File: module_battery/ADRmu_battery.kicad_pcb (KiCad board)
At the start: 2 copper layers, 160 x 100 mm, 81 parts, among them J101 Harting 09042326831, Q101 Q_NMOS_GDS, Q102 Q_NMOS_GDS, Q103 MMBFJ111, Q104 MMBFJ111, Q105 MMBFJ111, Q106 MMBFJ111, U101 BQ7791500, U102 LTC4079, U103 L7812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

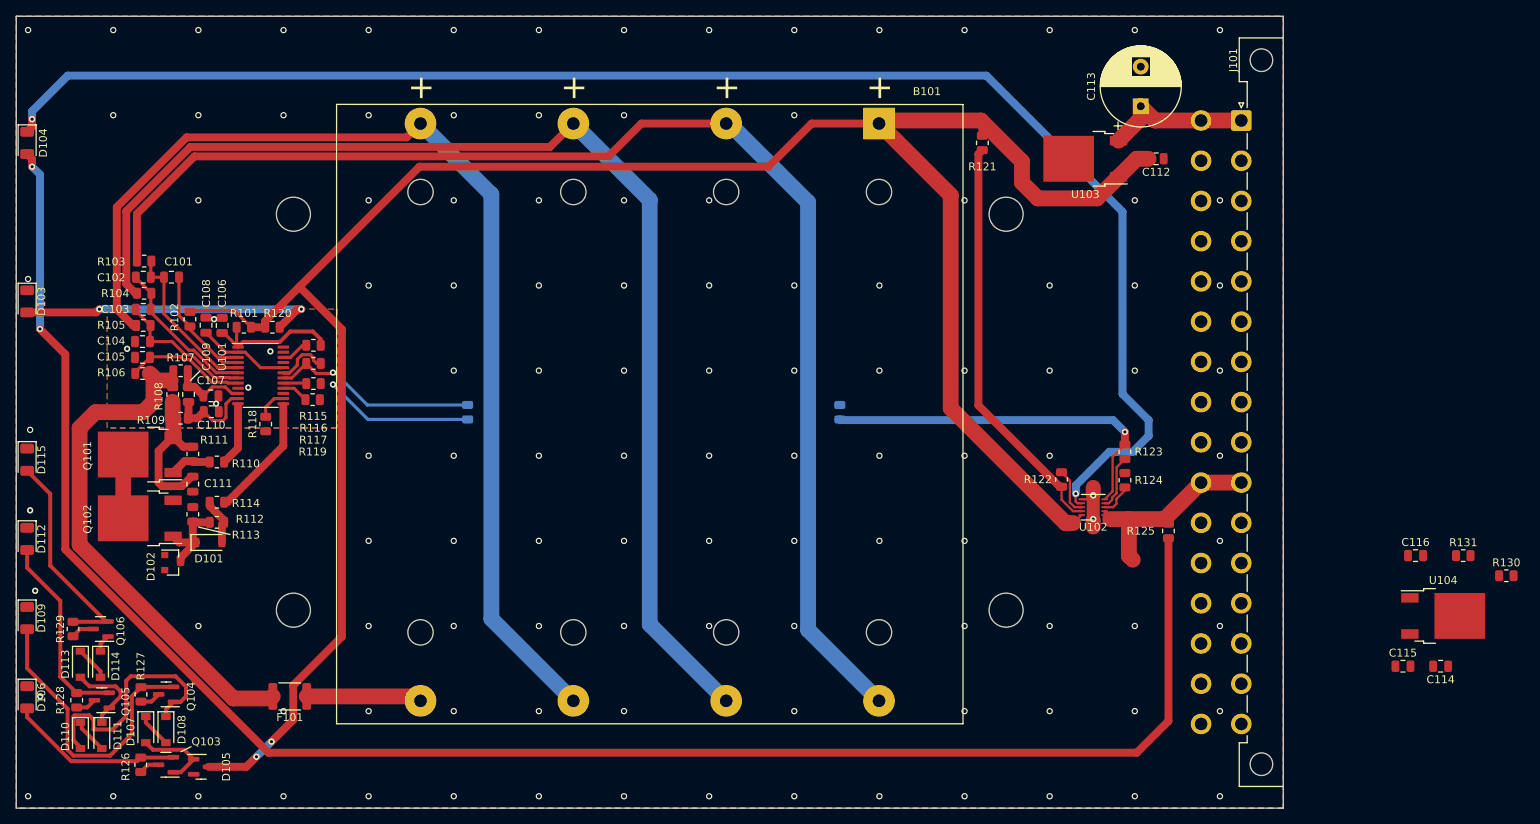
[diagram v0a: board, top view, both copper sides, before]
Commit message: battery module rev 0.3 routed
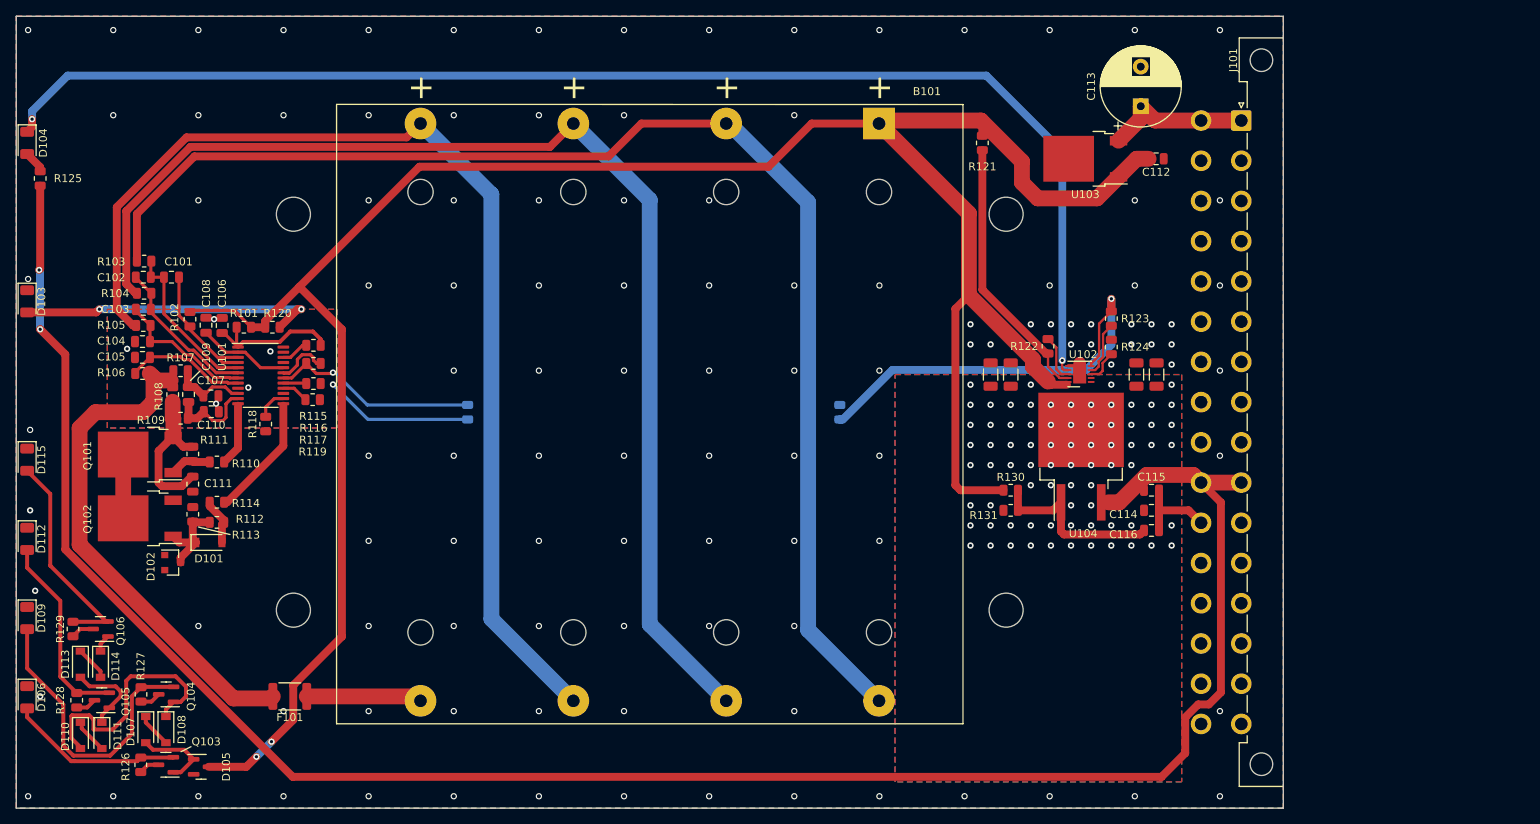
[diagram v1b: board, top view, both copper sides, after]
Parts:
- added HS101: THJP1206AST1, Capacitor_SMD:C_1206_3216Metric, F.Cu at (193.0, 95.2)
- added HS102: THJP1206AST1, Capacitor_SMD:C_1206_3216Metric, F.Cu at (195.6, 95.2)
- added HS103: THJP1206AST1, Capacitor_SMD:C_1206_3216Metric, F.Cu at (211.5, 95.2)
- added HS104: THJP1206AST1, Capacitor_SMD:C_1206_3216Metric, F.Cu at (214.0, 95.2)
- U104: value LM317_TO-252 -> LM317_TO-263; footprint Package_TO_SOT_SMD:TO-252-2 -> Package_TO_SOT_SMD:TO-263-2
- moved R125 149.3 mm to (73.0, 70.5), turned to 90 degrees
- moved R130 63.5 mm to (195.6, 109.9), turned to 180 degrees
- moved R131 57.4 mm to (195.6, 112.4)
- moved U104 50.0 mm to (204.5, 105.6), turned to 90 degrees
- moved C114 41.5 mm to (213.4, 112.4), turned to 0 degrees
- moved C115 38.8 mm to (213.4, 109.9)
- moved C116 33.5 mm to (213.4, 114.9)
- moved R124 16.9 mm to (208.3, 91.8)
- moved R122 16.9 mm to (200.3, 91.7)
- moved R123 16.9 mm to (208.3, 88.2)
- moved U102 16.9 mm to (204.3, 95.2)
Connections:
- net Net-(U102-Pad1) renamed /dropped_in+
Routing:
- net /in+: track 24.4 -> 258.4 mm, vias 0 -> 2
- net Net-(D104-Pad2): track 226.6 -> 2.86 mm, vias 2 -> 0
- net Net-(D104-Pad1): track 193.9 -> 167.0 mm
- net Net-(C116-Pad1): track 0.00 -> 22.9 mm
- net Net-(R121-Pad1): track 52.0 -> 34.0 mm
- net +BATT: track 278.0 -> 290.4 mm
- net /-i/o: track 6.46 -> 14.0 mm
- net Net-(R123-Pad1): track 46.2 -> 53.7 mm
- net /dropped_in+: vias 0 -> 75
- added copper zone on B.Cu, net /dropped_in+
- added copper zone on F.Cu, net /dropped_in+
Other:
- board text added: "ADRmu Battery module Rev 0.3"
- board text removed: "ADRmu Battery module Rev 0.2"

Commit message: Battery module Rev 0.4 routed
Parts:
- removed D107, D108, D110, D111, D113, D114: 1N4148, Diode_SMD:D_SOD-123
- removed D115: LT Y8SG-V2AB-36, LED_SMD:LED_1206_3216Metric
- removed Q103, Q104, Q105, Q106: MMBFJ111, Package_TO_SOT_SMD:SOT-23
- added C117: 100n 50V, Capacitor_SMD:C_0805_2012Metric, F.Cu at (84.5, 130.8)
- added D116: RS1D-13-F, Diode_SMD:D_SMA, F.Cu at (214.0, 106.7)
- added R132: 33k, Resistor_SMD:R_0805_2012Metric, F.Cu at (79.4, 131.7)
- added R133: 1k8, Resistor_SMD:R_0805_2012Metric, F.Cu at (79.4, 135.3)
- added R134: 1k8, Resistor_SMD:R_0805_2012Metric, F.Cu at (79.4, 138.7)
- added R135: 68k, Resistor_SMD:R_0805_2012Metric, F.Cu at (79.4, 142.2)
- added R136: 10k, Resistor_SMD:R_0805_2012Metric, F.Cu at (89.5, 135.5)
- added R137: 10k, Resistor_SMD:R_0805_2012Metric, F.Cu at (89.5, 139.1)
- added U105: LM339, Package_SO:SOIC-14_3.9x8.7mm_P1.27mm, F.Cu at (84.5, 136.5)
- R126, R127, R128: value 5k1 -> 49k9
- R129: value 1k2 -> 10k
- moved R129 27.1 mm to (98.4, 144.1), turned to 0 degrees
- moved R128 17.1 mm to (71.8, 120.4)
- moved R127 15.0 mm to (71.8, 130.2)
- moved R126 14.7 mm to (71.8, 140.1)
- moved D105 1.27 mm to (94.6, 144.8)
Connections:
- C115 pad 1: /in+ -> Net-(C115-Pad1)
- D105 pad 1: Net-(D105-Pad1) -> /-i/o
- D105 pad 3: +BATT -> Net-(R132-Pad2)
- D106 pad 1: /-i/o -> Net-(D106-Pad1)
- D109 pad 1: /-i/o -> Net-(D109-Pad1)
- D112 pad 1: /-i/o -> Net-(D112-Pad1)
- R125 pad 1: /in+ -> Net-(C115-Pad1)
- R126 pad 2: Net-(Q103-Pad3) -> +BATT
- R127 pad 2: Net-(Q104-Pad3) -> +BATT
- R128 pad 2: Net-(Q105-Pad3) -> +BATT
- R129 pad 1: Net-(D115-Pad2) -> Net-(R132-Pad2)
- R129 pad 2: Net-(Q106-Pad3) -> +BATT
- U104 pad 3: /in+ -> Net-(C115-Pad1)
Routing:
- net Net-(C115-Pad1): track 0.00 -> 257.5 mm, vias 0 -> 2
- net /in+: track 258.4 -> 9.62 mm, vias 2 -> 0
- net +BATT: track 290.4 -> 371.2 mm, vias 2 -> 7
- net Net-(D109-Pad2): track 37.4 -> 2.02 mm
- net Net-(R132-Pad2): track 0.00 -> 33.4 mm
- net Net-(D108-Pad1): track 31.9 -> 0.00 mm
- net Net-(D115-Pad2): track 27.8 -> 0.00 mm
- net Net-(D112-Pad1): track 0.00 -> 27.8 mm
- net Net-(D112-Pad2): track 24.8 -> 2.22 mm
- net Net-(D106-Pad2): track 22.1 -> 1.90 mm
- net Net-(D109-Pad1): track 0.00 -> 15.0 mm
- net Net-(D106-Pad1): track 0.00 -> 14.5 mm, vias 0 -> 2
- net Net-(R136-Pad1): track 0.00 -> 13.7 mm
- net Net-(R134-Pad1): track 0.00 -> 12.6 mm, vias 0 -> 2
- net Net-(D111-Pad1): track 10.7 -> 0.00 mm
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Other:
- board text added: "ADRmu Battery module Rev 0.4"
- board text removed: "ADRmu Battery module Rev 0.3"

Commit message: Battery module Rev 0.6 update
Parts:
- removed R123: 10k, Resistor_SMD:R_0805_2012Metric
- H101, H102, H103, H104: footprint MountingHole:MountingHole_4.3mm_M4 -> MountingHole:MountingHole_5.3mm_M5
- R132: value 33k -> 22k
- R133, R134: value 1k8 -> 6k8
- R135: value 68k -> 82k
- TH102: value CMFB3435103FNT -> Alternative 10k NTC; footprint Resistor_SMD:R_0805_2012Metric -> Resistor_THT:R_Axial_DIN0204_L3.6mm_D1.6mm_P2.54mm_Vertical; moved to F.Cu
- moved TH102 65.7 mm to (108.4, 103.3), turned to 90 degrees
- renumbered D112 to D106, D106 to D112, R128 to R126, R126 to R128
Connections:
- D106 pad 1: Net-(D112-Pad1) -> Net-(D106-Pad1)
- D112 pad 1: Net-(D106-Pad1) -> Net-(D112-Pad1)
- TH102 pad 1: /-i/o -> Net-(R116-Pad1)
- TH102 pad 2: Net-(R123-Pad1) -> GND
- U102 pad 4: Net-(R123-Pad2) -> unconnected-(U102-Pad4)
- U102 pad 5: Net-(R123-Pad1) -> /-i/o
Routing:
- net Net-(R123-Pad1): track 53.7 -> 0.00 mm, vias 1 -> 0
- net +BATT: track 371.2 -> 353.0 mm
- net Net-(D112-Pad1): track 27.8 -> 17.0 mm, vias 0 -> 2
- net Net-(D106-Pad1): track 14.5 -> 25.3 mm
- net Net-(R116-Pad1): track 26.3 -> 35.6 mm
- net Net-(R123-Pad2): track 6.94 -> 0.00 mm
- net /-i/o: track 14.0 -> 15.6 mm, vias 115 -> 114
- net Net-(R121-Pad1): track 34.0 -> 35.3 mm
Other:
- board text added: "ADRmu Battery module Rev 0.6"
- board text removed: "ADRmu Battery module Rev 0.4"
